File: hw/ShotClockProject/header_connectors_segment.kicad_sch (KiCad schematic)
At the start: 4 parts, among them J10 DW254W-22-20-85, J7 DW254W-22-20-85, J8 DW254W-22-20-85, J9 DW254W-22-20-85

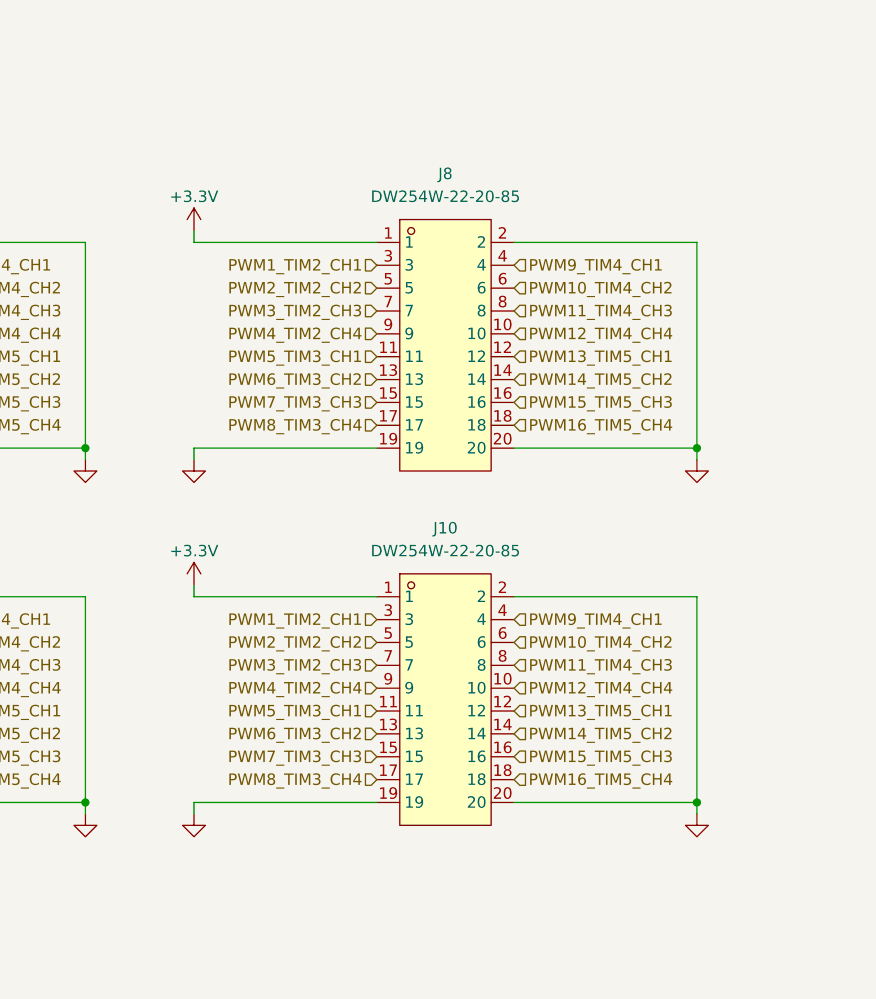
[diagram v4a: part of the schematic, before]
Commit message: Finished rough layout of PCB (ready for review)
Changed battery polarity to match the batteries I have.
Added power led to voltage regulator
Removed old comments from schematic
Gave all footprints a 3D model
Replaced batttery footprint with a SMD JST 3 pins horizontal connector
Finished rough placement of components
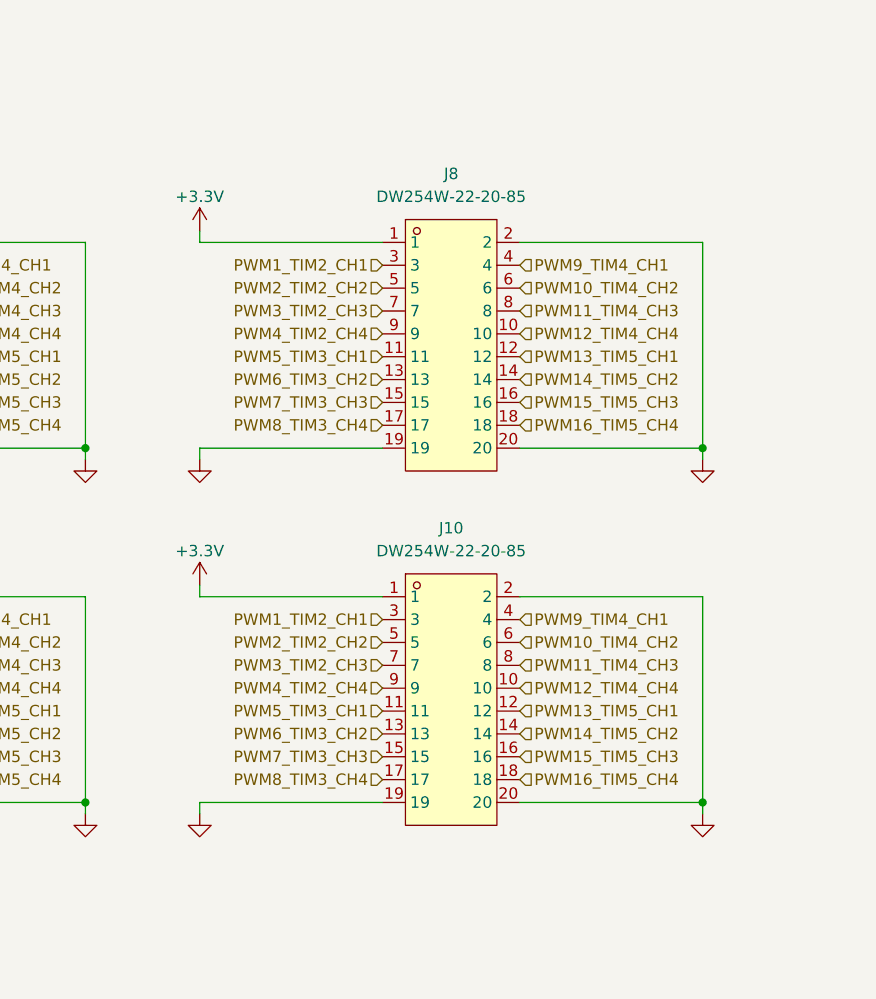
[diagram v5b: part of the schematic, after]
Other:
- moved on the sheet: J10, J8

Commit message: First feedback round from Luc on schematic
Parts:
- added C12: 10n, Capacitor_SMD:C_0603_1608Metric, symbol Device:C
- added D1: Orange LED, LED_SMD:LED_0603_1608Metric, symbol Device:LED
- added Q1 (x2): Q_NPN_BCE, Package_TO_SOT_SMD:SOT-23, symbol Device:Q_NPN_BCE
- added Q1: Q_PMOS_SGD, symbol Device:Q_PMOS_SGD
- added R2: 1k, Resistor_SMD:R_0402_1005Metric, symbol Device:R
- added R2 (x2): 10k, Resistor_SMD:R_0402_1005Metric, symbol Device:R
- added R2: 100k, Resistor_SMD:R_0402_1005Metric, symbol Device:R
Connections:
- net +3.3V: now also Q1.1 (S), R2.2
- net GND: now also C12.2, Q1.3 (E), Q1.3 (E), R2.1
- net PWM1_TIM2_CH1: now also R2.2
- new net: C12.1, Q1.1 (B), R2.1, R2.2
- new net: Q1.2 (C), Q1.2 (G), R2.1
- new net: D1.1 (K), Q1.2 (C)
- new net: D1.2 (A), R2.1
- new net: Q1.3 (D), R2.2
- new net D_IO_1: Q1.1 (B)

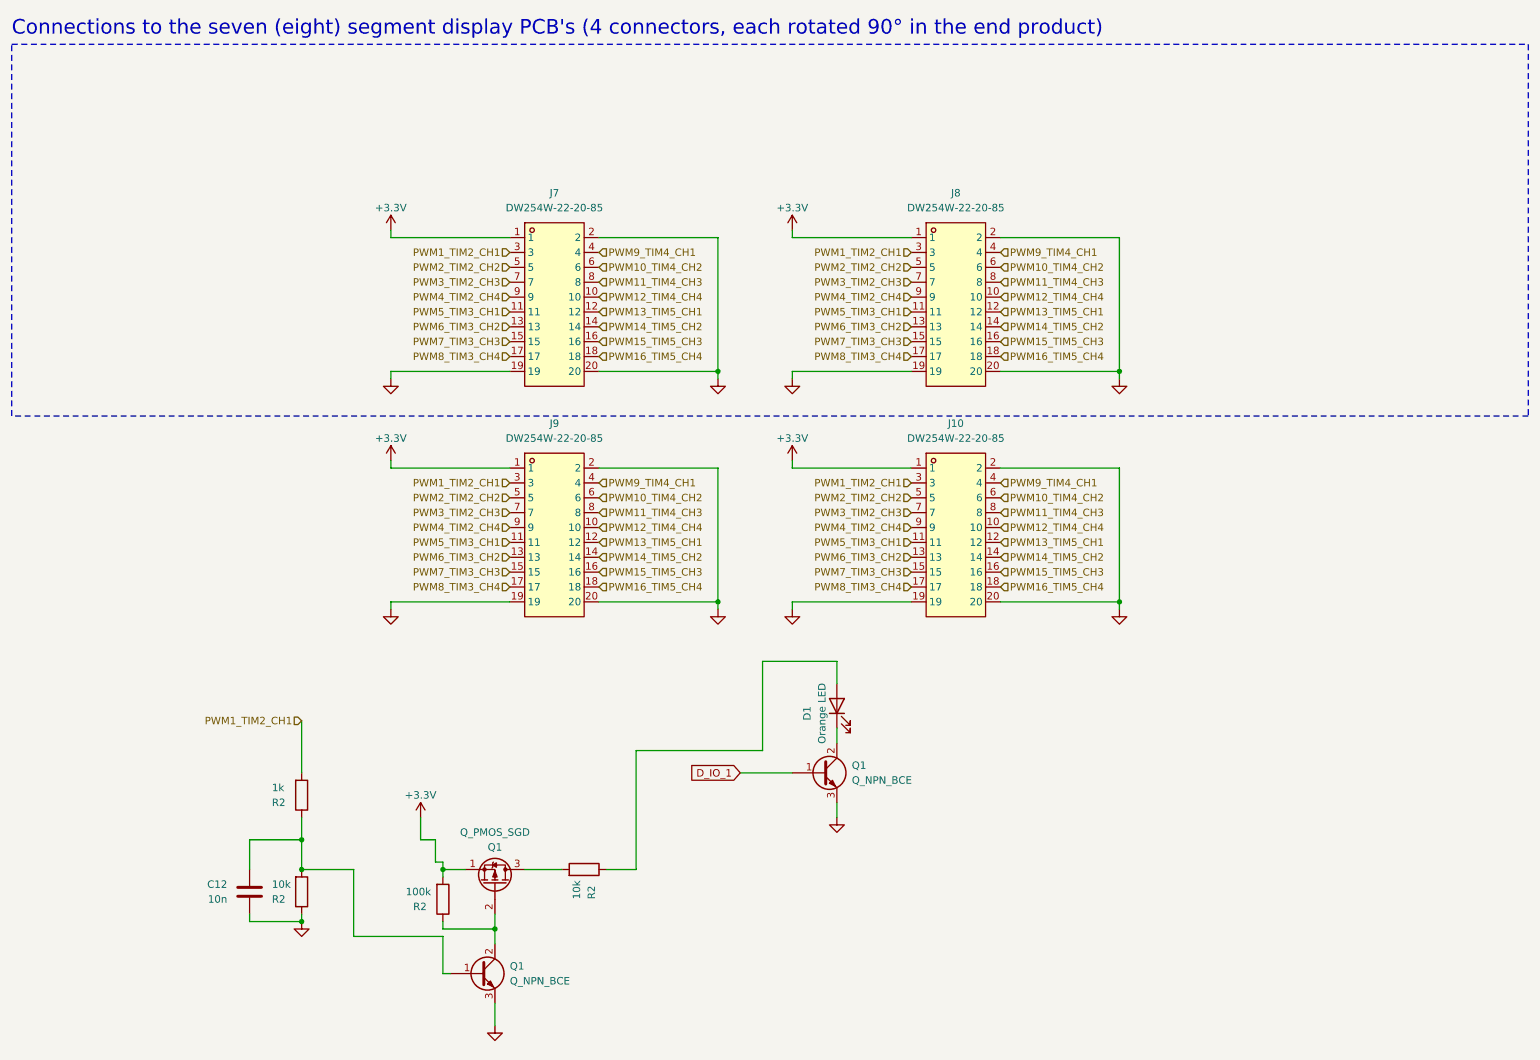
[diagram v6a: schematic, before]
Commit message: Changed pinouts
To only use 1 pwm per display, and GPIo outs for the rest in both HW and firmware
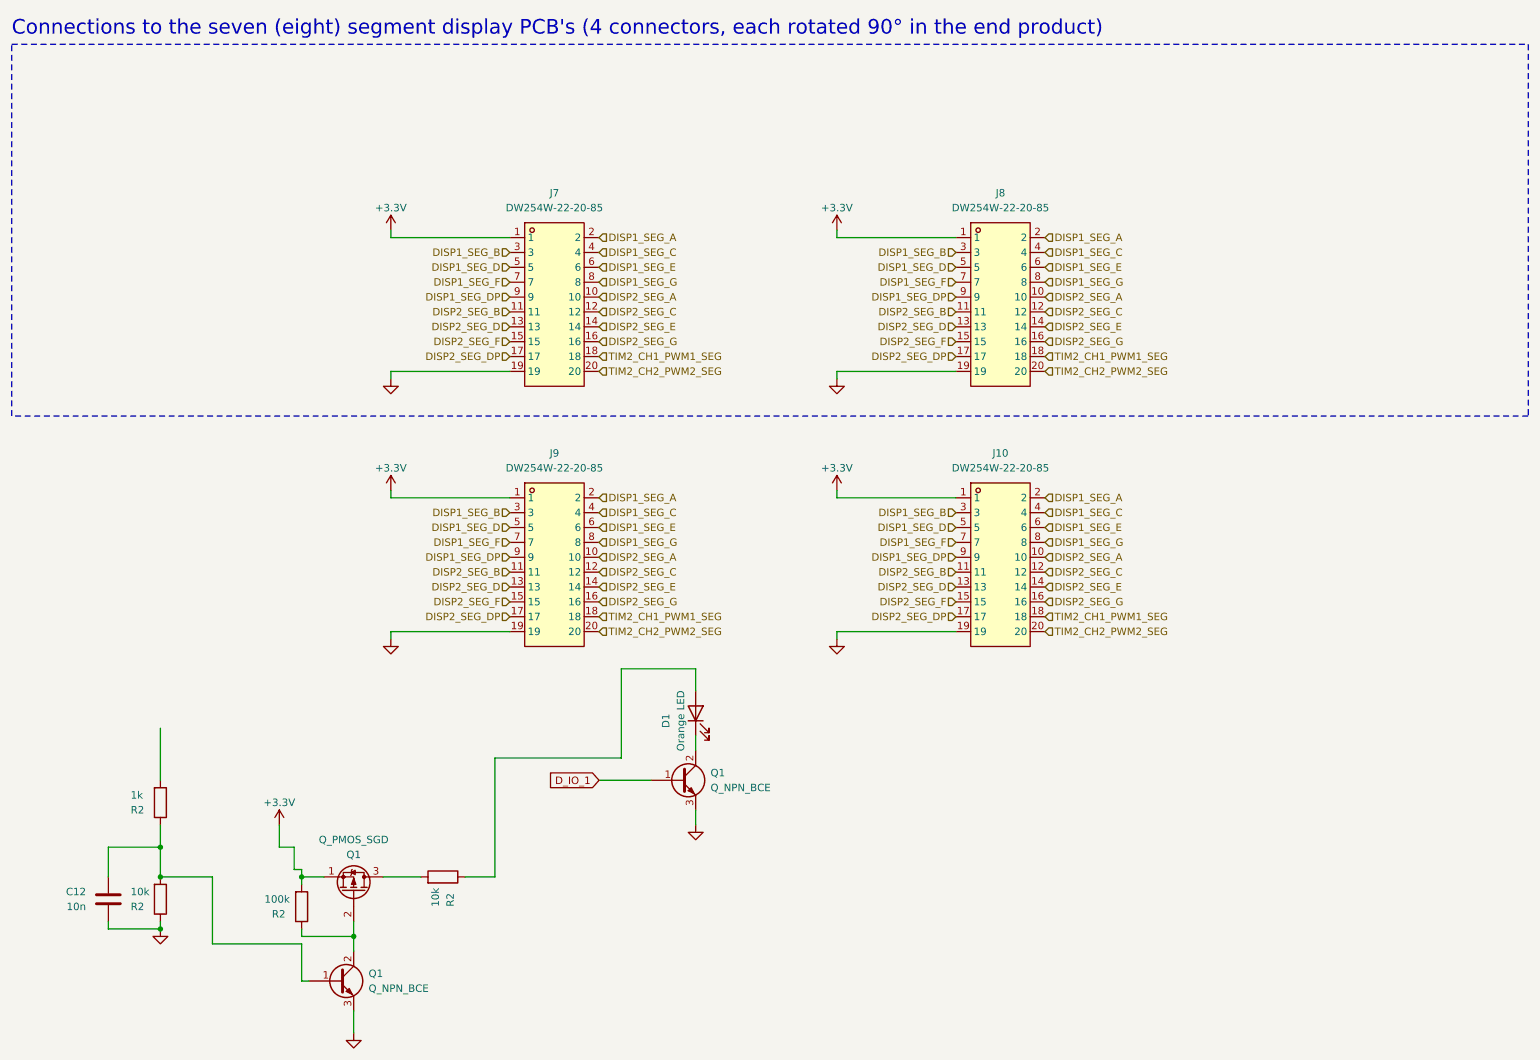
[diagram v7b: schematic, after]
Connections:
- net GND: no longer J10.2, J10.20, J7.2, J7.20, J8.2, J8.20, J9.2, J9.20
- net PWM10_TIM4_CH2 renamed DISP1_SEG_E
- net PWM11_TIM4_CH3 renamed DISP1_SEG_G
- net PWM12_TIM4_CH4 renamed DISP2_SEG_A
- net PWM13_TIM5_CH1 renamed DISP2_SEG_C
- net PWM14_TIM5_CH2 renamed DISP2_SEG_E
- net PWM15_TIM5_CH3 renamed DISP2_SEG_G
- net PWM16_TIM5_CH4 renamed TIM2_CH1_PWM1_SEG
- net PWM1_TIM2_CH1 renamed DISP1_SEG_B
- net DISP1_SEG_B: no longer R2.2
- net PWM2_TIM2_CH2 renamed DISP1_SEG_D
- net PWM3_TIM2_CH3 renamed DISP1_SEG_F
- net PWM4_TIM2_CH4 renamed DISP1_SEG_DP
- net PWM5_TIM3_CH1 renamed DISP2_SEG_B
- net PWM6_TIM3_CH2 renamed DISP2_SEG_D
- net PWM7_TIM3_CH3 renamed DISP2_SEG_F
- net PWM8_TIM3_CH4 renamed DISP2_SEG_DP
- net PWM9_TIM4_CH1 renamed DISP1_SEG_C
- new net DISP1_SEG_A: J10.2, J7.2, J8.2, J9.2
- new net TIM2_CH2_PWM2_SEG: J10.20, J7.20, J8.20, J9.20
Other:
- moved on the sheet: C12, D1, Q1, R2

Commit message: Started on second PCB, and added 5V regulator
5V regulator added to main pcb for the segment displays, using same TPS63000 chip, but with a different selector resistor to choose for 5V

Added second project to contain the display PCBA design.

Calculated the current usage of the displays with different current limiting resistors on the LEDs.

Calculated the  current limit resistors for transistors behind LEDs
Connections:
- net +3.3V: no longer J10.1, J7.1, J8.1, J9.1
- new net +5V: J10.1, J7.1, J8.1, J9.1
